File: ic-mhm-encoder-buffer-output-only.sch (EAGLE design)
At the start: 35 parts, among them IC1 LS7183-SOIC, J1 2023960907, J2 2023960607, M1 BSS670S2LH6327XTSA1, SW1 CS-4-13NTA, U1 24LC16BT-I/MC, U2 D5V0F4U6S-7, U3 D5V0F4U6S-7, U4 D5V0F4U6S-7

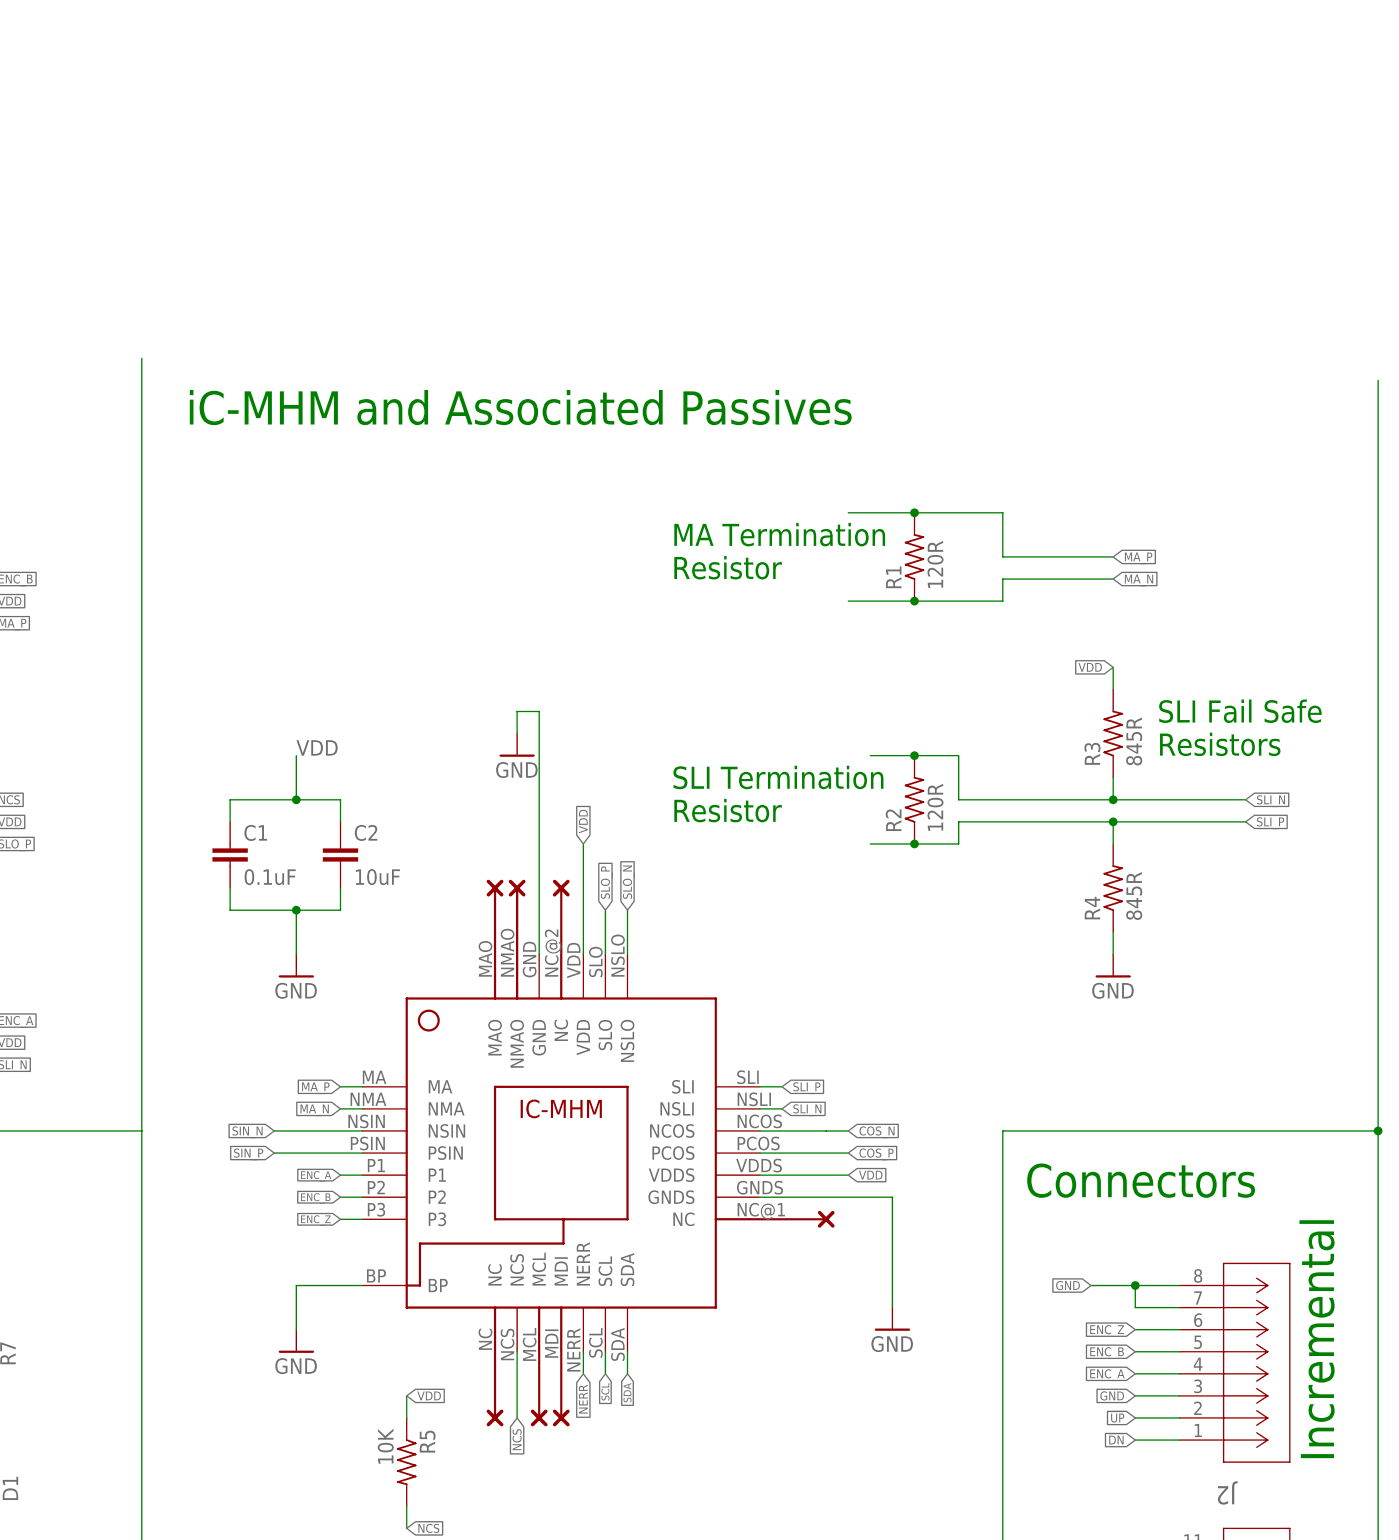
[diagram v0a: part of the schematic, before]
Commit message: added verisons with buffers on ABI
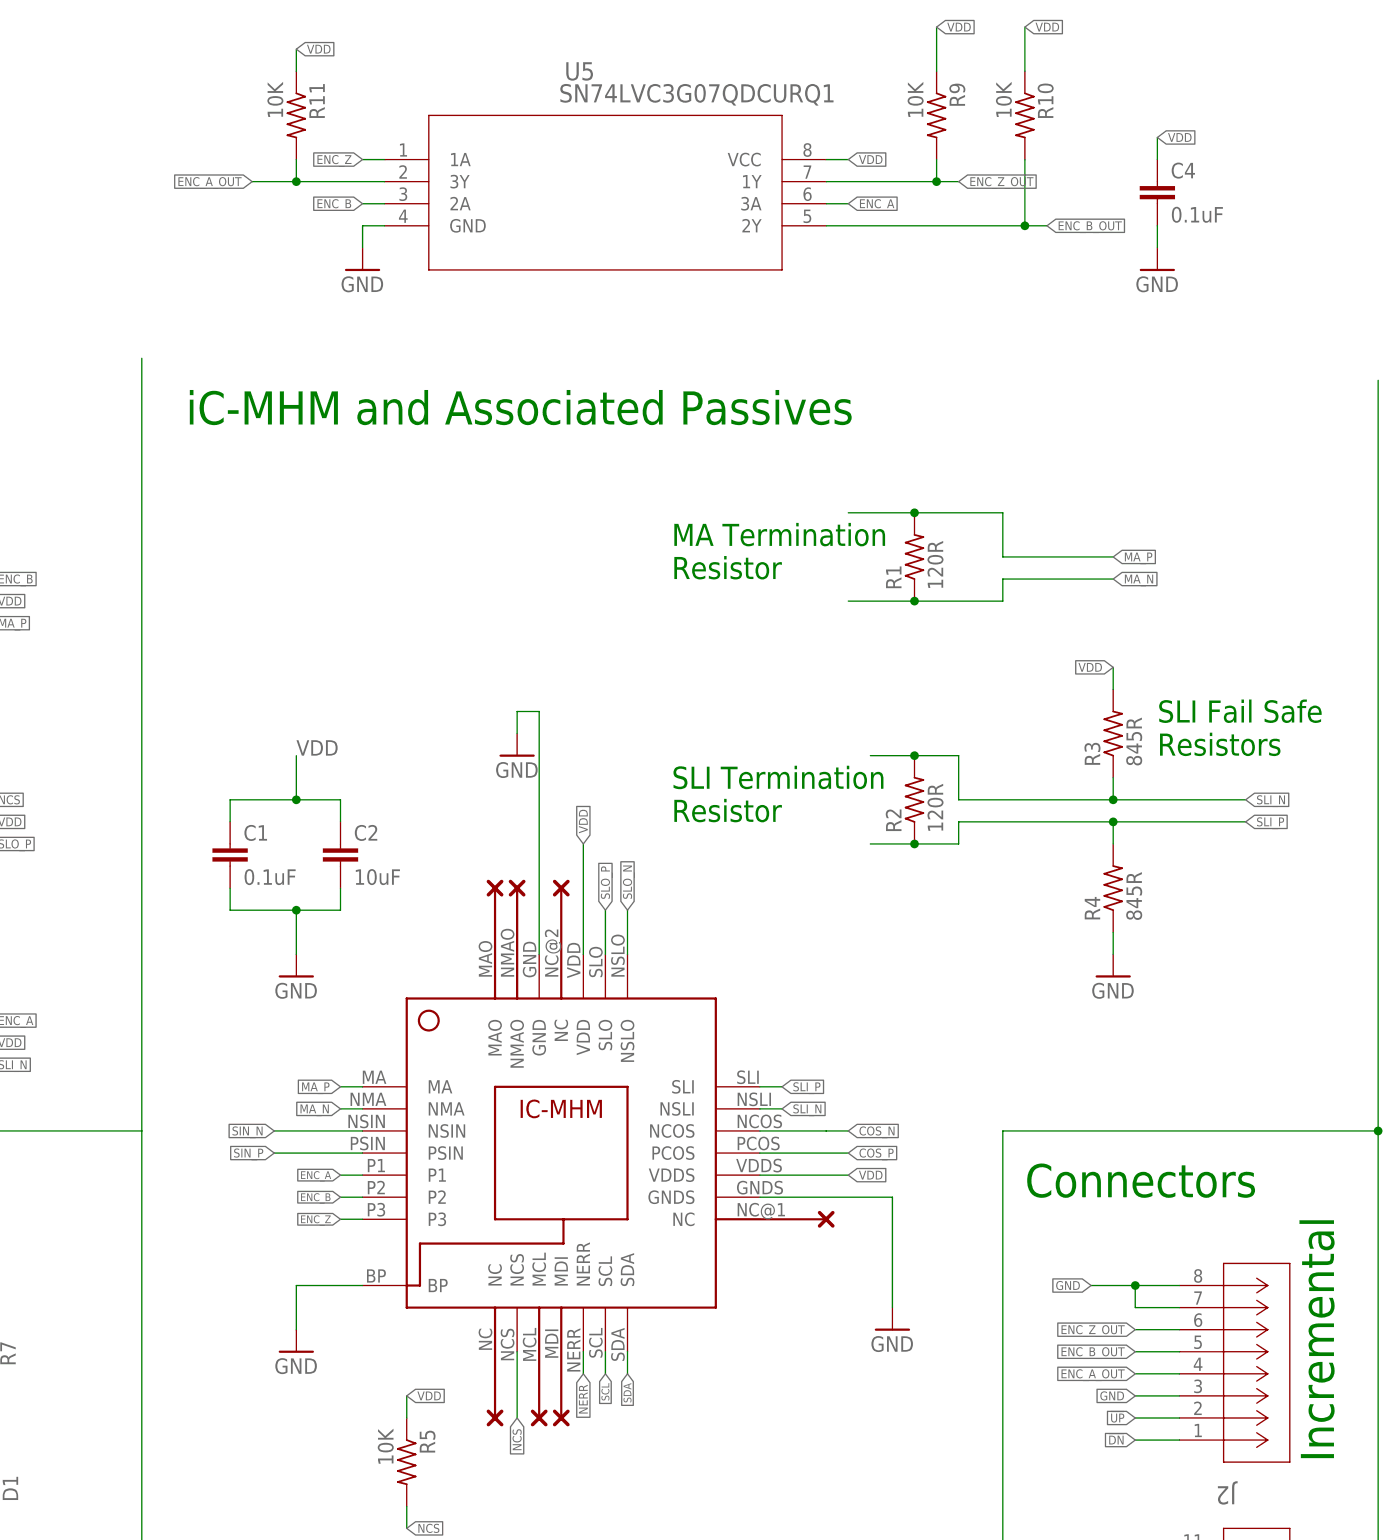
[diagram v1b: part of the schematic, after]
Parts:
- added C4: 0.1uF, rcl:C-EUC0603
- added R10, R11, R9: 10K, rcl:R-US_R0603
- added U5: SN74LVC3G07QDCURQ1, ic-mhm:SN74LVC3G07QDCURQ1
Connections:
- new net ENC_A_OUT: J2.4, R11.2, U5.3Y
- new net ENC_B_OUT: J2.5, R10.2, U5.2Y
- new net ENC_Z_OUT: J2.6, R9.2, U5.1Y
- net ENC_A: now also U5.3A; no longer J2.4
- net ENC_B: now also U5.2A; no longer J2.5
- net ENC_Z: now also U5.1A; no longer J2.6
- net GND: now also C4.2, U5.GND
- net VDD: now also C4.1, R10.1, R11.1, R9.1, U5.VCC
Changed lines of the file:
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@@
 <part name="GND14" library="supply1" library_urn="urn:adsk.eagle:library:371" deviceset="GND" device=""/>
 <part name="GND15" library="supply1" library_urn="urn:adsk.eagle:library:371" deviceset="GND" device=""/>
+<part name="U5" library="ic-mhm" library_urn="urn:adsk.eagle:library:32396126" deviceset="SN74LVC3G07QDCURQ1" device="" package3d_urn="urn:adsk.eagle:package:32720582/1"/>
+<part name="R9" library="rcl" library_urn="urn:adsk.eagle:library:334" deviceset="R-US_" device="R0603" package3d_urn="urn:adsk.eagle:package:23555/3" value="10K"/>
+<part name="R10" library="rcl" library_urn="urn:adsk.eagle:library:334" deviceset="R-US_" device="R0603" package3d_urn="urn:adsk.eagle:package:23555/3" value="10K"/>
+<part name="R11" library="rcl" library_urn="urn:adsk.eagle:library:334" deviceset="R-US_" device="R0603" package3d_urn="urn:adsk.eagle:package:23555/3" value="10K"/>
+<part name="GND16" library="supply1" library_urn="urn:adsk.eagle:library:371" deviceset="GND" device=""/>
+<part name="GND17" library="supply1" library_urn="urn:adsk.eagle:library:371" deviceset="GND" device=""/>
+<part name="C4" library="rcl" library_urn="urn:adsk.eagle:library:334" deviceset="C-EU" device="C0603" package3d_urn="urn:adsk.eagle:package:23616/2" value="0.1uF"/>
 </parts>
 <sheets>
@@
 <attribute name="VALUE" x="5.08" y="121.92" size="1.778" layer="96"/>
 </instance>
+<instance part="U5" gate="A" x="116.84" y="231.14" smashed="yes">
+<attribute name="NAME" x="140.0556" y="240.2586" size="2.0828" layer="95" ratio="6" rot="SR0"/>
+<attribute name="VALUE" x="139.4206" y="237.7186" size="2.0828" layer="96" ratio="6" rot="SR0"/>
+</instance>
+<instance part="R9" gate="G$1" x="182.88" y="236.22" smashed="yes" rot="R270">
+<attribute name="NAME" x="184.3786" y="240.03" size="1.778" layer="95" rot="R270"/>
+<attribute name="VALUE" x="179.578" y="240.03" size="1.778" layer="96" rot="R270"/>
+</instance>
+<instance part="R10" gate="G$1" x="193.04" y="236.22" smashed="yes" rot="R270">
+<attribute name="NAME" x="194.5386" y="240.03" size="1.778" layer="95" rot="R270"/>
+<attribute name="VALUE" x="189.738" y="240.03" size="1.778" layer="96" rot="R270"/>
+</instance>
+<instance part="R11" gate="G$1" x="109.22" y="236.22" smashed="yes" rot="R270">
+<attribute name="NAME" x="110.7186" y="240.03" size="1.778" layer="95" rot="R270"/>
+<attribute name="VALUE" x="105.918" y="240.03" size="1.778" layer="96" rot="R270"/>
+</instance>
+<instance part="GND16" gate="1" x="116.84" y="218.44" smashed="yes">
+<attribute name="VALUE" x="114.3" y="215.9" size="1.778" layer="96"/>
+</instance>
+<instance part="GND17" gate="1" x="208.28" y="218.44" smashed="yes">
+<attribute name="VALUE" x="205.74" y="215.9" size="1.778" layer="96"/>
+</instance>
+<instance part="C4" gate="G$1" x="208.28" y="228.6" smashed="yes">
+<attribute name="NAME" x="209.804" y="228.981" size="1.778" layer="95"/>
+<attribute name="VALUE" x="209.804" y="223.901" size="1.778" layer="96"/>
+</instance>
 </instances>
 <busses>
@@
 </segment>
 <segment>
-<pinref part="J2" gate="A" pin="4"/>
-<wire x1="210.82" y1="91.44" x2="205.74" y2="91.44" width="0.1524" layer="91"/>
-<label x="205.74" y="91.44" size="1.016" layer="95" rot="R180" xref="yes"/>
-</segment>
-<segment>
 <pinref part="U4" gate="A" pin="CH4"/>
 <wire x1="71.12" y1="132.08" x2="73.66" y2="132.08" width="0.1524" layer="91"/>
@@
 <label x="114.3" y="114.3" size="0.889" layer="95" rot="R180" xref="yes"/>
 </segment>
+<segment>
+<pinref part="U5" gate="A" pin="3A"/>
+<wire x1="170.18" y1="226.06" x2="172.72" y2="226.06" width="0.1524" layer="91"/>
+<label x="172.72" y="226.06" size="1.016" layer="95" xref="yes"/>
+</segment>
 </net>
 <net name="ENC_B" class="0">
@@
 </segment>
 <segment>
-<pinref part="J2" gate="A" pin="5"/>
-<wire x1="210.82" y1="93.98" x2="205.74" y2="93.98" width="0.1524" layer="91"/>
-<label x="205.74" y="93.98" size="1.016" layer="95" rot="R180" xref="yes"/>
-</segment>
-<segment>
 <pinref part="U2" gate="A" pin="CH4"/>
 <wire x1="71.12" y1="182.88" x2="73.66" y2="182.88" width="0.1524" layer="91"/>
@@
 <label x="114.3" y="111.76" size="0.889" layer="95" rot="R180" xref="yes"/>
 </segment>
+<segment>
+<pinref part="U5" gate="A" pin="2A"/>
+<wire x1="119.38" y1="226.06" x2="116.84" y2="226.06" width="0.1524" layer="91"/>
+<label x="116.84" y="226.06" size="1.016" layer="95" rot="R180" xref="yes"/>
+</segment>
 </net>
 <net name="ENC_Z" class="0">
@@
 </segment>
 <segment>
-<pinref part="J2" gate="A" pin="6"/>
-<wire x1="210.82" y1="96.52" x2="205.74" y2="96.52" width="0.1524" layer="91"/>
-<label x="205.74" y="96.52" size="1.016" layer="95" rot="R180" xref="yes"/>
-</segment>
-<segment>
 <pinref part="U2" gate="A" pin="CH1"/>
 <wire x1="20.32" y1="182.88" x2="17.78" y2="182.88" width="0.1524" layer="91"/>
@@
 <wire x1="116.84" y1="109.22" x2="114.3" y2="109.22" width="0.1524" layer="91"/>
 <label x="114.3" y="109.22" size="0.889" layer="95" rot="R180" xref="yes"/>
+</segment>
+<segment>
+<pinref part="U5" gate="A" pin="1A"/>
+<wire x1="119.38" y1="231.14" x2="116.84" y2="231.14" width="0.1524" layer="91"/>
+<label x="116.84" y="231.14" size="1.016" layer="95" rot="R180" xref="yes"/>
 </segment>
 </net>
@@
 <pinref part="GND15" gate="1" pin="GND"/>
 </segment>
+<segment>
+<pinref part="U5" gate="A" pin="GND"/>
+<wire x1="119.38" y1="223.52" x2="116.84" y2="223.52" width="0.1524" layer="91"/>
+<wire x1="116.84" y1="223.52" x2="116.84" y2="220.98" width="0.1524" layer="91"/>
+<pinref part="GND16" gate="1" pin="GND"/>
+</segment>
+<segment>
+<wire x1="208.28" y1="223.52" x2="208.28" y2="220.98" width="0.1524" layer="91"/>
+<pinref part="GND17" gate="1" pin="GND"/>
+<pinref part="C4" gate="G$1" pin="2"/>
+</segment>
 </net>
 <net name="VDD" class="0">
@@
 <wire x1="71.12" y1="129.54" x2="73.66" y2="129.54" width="0.1524" layer="91"/>
 <label x="73.66" y="129.54" size="1.016" layer="95" xref="yes"/>
+</segment>
+<segment>
+<pinref part="R11" gate="G$1" pin="1"/>
+<wire x1="109.22" y1="241.3" x2="109.22" y2="243.84" width="0.1524" layer="91"/>
+<label x="109.22" y="243.84" size="1.016" layer="95" xref="yes"/>
+</segment>
+<segment>
+<pinref part="R9" gate="G$1" pin="1"/>
+<wire x1="182.88" y1="241.3" x2="182.88" y2="246.38" width="0.1524" layer="91"/>
+<label x="182.88" y="246.38" size="1.016" layer="95" xref="yes"/>
+</segment>
+<segment>
+<pinref part="R10" gate="G$1" pin="1"/>
+<wire x1="193.04" y1="241.3" x2="193.04" y2="246.38" width="0.1524" layer="91"/>
+<label x="193.04" y="246.38" size="1.016" layer="95" xref="yes"/>
+</segment>
+<segment>
+<pinref part="U5" gate="A" pin="VCC"/>
+<wire x1="170.18" y1="231.14" x2="172.72" y2="231.14" width="0.1524" layer="91"/>
+<label x="172.72" y="231.14" size="1.016" layer="95" xref="yes"/>
+</segment>
+<segment>
+<wire x1="208.28" y1="231.14" x2="208.28" y2="233.68" width="0.1524" layer="91"/>
+<label x="208.28" y="233.68" size="1.016" layer="95" xref="yes"/>
+<pinref part="C4" gate="G$1" pin="1"/>
 </segment>
 </net>
@@
 </segment>
 </net>
+<net name="ENC_A_OUT" class="0">
+<segment>
+<pinref part="U5" gate="A" pin="3Y"/>
+<wire x1="119.38" y1="228.6" x2="109.22" y2="228.6" width="0.1524" layer="91"/>
+<pinref part="R11" gate="G$1" pin="2"/>
+<wire x1="109.22" y1="228.6" x2="104.14" y2="228.6" width="0.1524" layer="91"/>
+<wire x1="109.22" y1="231.14" x2="109.22" y2="228.6" width="0.1524" layer="91"/>
+<junction x="109.22" y="228.6"/>
+<label x="104.14" y="228.6" size="1.016" layer="95" rot="R180" xref="yes"/>
+</segment>
+<segment>
+<pinref part="J2" gate="A" pin="4"/>
+<wire x1="210.82" y1="91.44" x2="205.74" y2="91.44" width="0.1524" layer="91"/>
+<label x="205.74" y="91.44" size="1.016" layer="95" rot="R180" xref="yes"/>
+</segment>
+</net>
+<net name="ENC_Z_OUT" class="0">
+<segment>
+<pinref part="U5" gate="A" pin="1Y"/>
+<wire x1="170.18" y1="228.6" x2="182.88" y2="228.6" width="0.1524" layer="91"/>
+<pinref part="R9" gate="G$1" pin="2"/>
+<wire x1="182.88" y1="228.6" x2="182.88" y2="231.14" width="0.1524" layer="91"/>
+<wire x1="182.88" y1="228.6" x2="185.42" y2="228.6" width="0.1524" layer="91"/>
+<junction x="182.88" y="228.6"/>
+<label x="185.42" y="228.6" size="1.016" layer="95" xref="yes"/>
+</segment>
+<segment>
+<pinref part="J2" gate="A" pin="6"/>
+<wire x1="210.82" y1="96.52" x2="205.74" y2="96.52" width="0.1524" layer="91"/>
+<label x="205.74" y="96.52" size="1.016" layer="95" rot="R180" xref="yes"/>
+</segment>
+</net>
+<net name="ENC_B_OUT" class="0">
+<segment>
+<pinref part="U5" gate="A" pin="2Y"/>
+<wire x1="170.18" y1="223.52" x2="193.04" y2="223.52" width="0.1524" layer="91"/>
+<pinref part="R10" gate="G$1" pin="2"/>
+<wire x1="193.04" y1="223.52" x2="193.04" y2="231.14" width="0.1524" layer="91"/>
+<wire x1="193.04" y1="223.52" x2="195.58" y2="223.52" width="0.1524" layer="91"/>
+<junction x="193.04" y="223.52"/>
+<label x="195.58" y="223.52" size="1.016" layer="95" xref="yes"/>
+</segment>
+<segment>
+<pinref part="J2" gate="A" pin="5"/>
+<wire x1="210.82" y1="93.98" x2="205.74" y2="93.98" width="0.1524" layer="91"/>
+<label x="205.74" y="93.98" size="1.016" layer="95" rot="R180" xref="yes"/>
+</segment>
+</net>
